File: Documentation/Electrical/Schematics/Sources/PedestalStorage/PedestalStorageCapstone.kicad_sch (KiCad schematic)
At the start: 2 parts

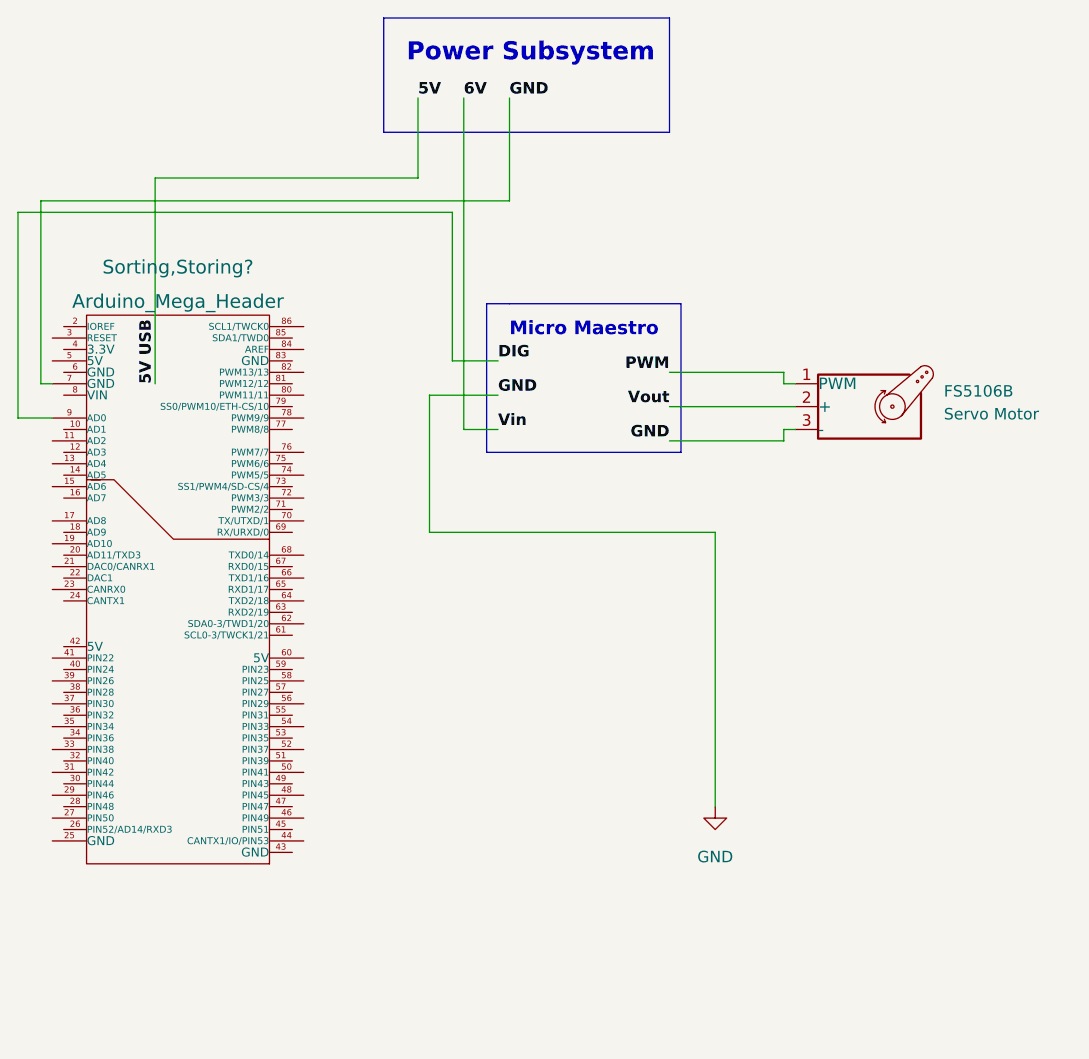
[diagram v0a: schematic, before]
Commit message: Deleted old circuit schenatic and added updated
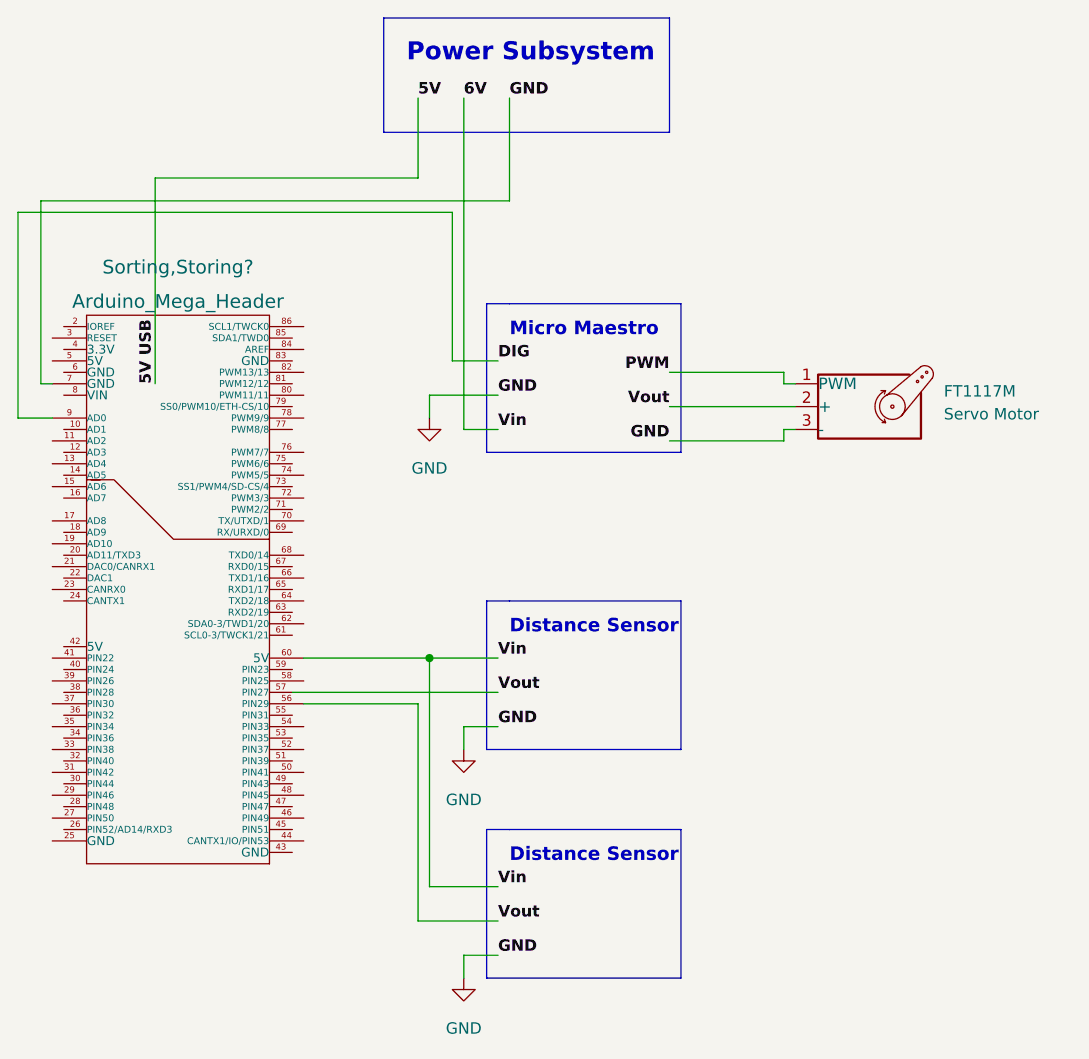
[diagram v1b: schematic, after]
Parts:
- renumbered FS5106B to FT1117M
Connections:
- net 6V: now also Sorting,Storing?.60 (5V)
- net Vout: now also Sorting,Storing?.56 (PIN29), Sorting,Storing?.57 (PIN27)
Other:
- note added: "Distance Sensor"
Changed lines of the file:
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@@
 (kicad_sch (version 20211123) (generator eeschema)
   (paper "A4")
+  (junction (at 99.06 102.87) (diameter 0) (color 0 0 0 0)
+  )
   (polyline (pts (xy 107.95 63.5) (xy 127 63.5))
     (stroke (width 0) (type solid) (color 0 0 0 0))
   )
+  (polyline (pts (xy 127 138.43) (xy 105.41 138.43))
+    (stroke (width 0) (type solid) (color 0 0 0 0))
+  )
   (wire (pts (xy 55.88 52.07) (xy 55.88 72.39))
     (stroke (width 0) (type default) (color 0 0 0 0))
@@
     (stroke (width 0) (type default) (color 0 0 0 0))
   )
-  (wire (pts (xy 130.81 88.9) (xy 130.81 119.38))
+  (wire (pts (xy 106.68 128.27) (xy 99.06 128.27))
+    (stroke (width 0) (type default) (color 0 0 0 0))
+  )
+  (wire (pts (xy 106.68 132.08) (xy 97.79 132.08))
     (stroke (width 0) (type default) (color 0 0 0 0))
   )
@@
     (stroke (width 0) (type default) (color 0 0 0 0))
   )
+  (polyline (pts (xy 127 121.92) (xy 127 138.43))
+    (stroke (width 0) (type solid) (color 0 0 0 0))
+  )
   (polyline (pts (xy 105.41 80.01) (xy 105.41 63.5))
     (stroke (width 0) (type solid) (color 0 0 0 0))
   )
-  (wire (pts (xy 99.06 88.9) (xy 130.81 88.9))
+  (polyline (pts (xy 105.41 113.03) (xy 105.41 96.52))
+    (stroke (width 0) (type solid) (color 0 0 0 0))
+  )
+  (wire (pts (xy 102.87 135.89) (xy 102.87 138.43))
     (stroke (width 0) (type default) (color 0 0 0 0))
   )
@@
     (stroke (width 0) (type default) (color 0 0 0 0))
   )
+  (polyline (pts (xy 127 113.03) (xy 105.41 113.03))
+    (stroke (width 0) (type solid) (color 0 0 0 0))
+  )
   (wire (pts (xy 57.15 76.2) (xy 53.34 76.2))
     (stroke (width 0) (type default) (color 0 0 0 0))
@@
     (stroke (width 0) (type default) (color 0 0 0 0))
   )
+  (wire (pts (xy 102.87 135.89) (xy 106.68 135.89))
+    (stroke (width 0) (type default) (color 0 0 0 0))
+  )
   (polyline (pts (xy 127 80.01) (xy 105.41 80.01))
     (stroke (width 0) (type solid) (color 0 0 0 0))
@@
     (stroke (width 0) (type default) (color 0 0 0 0))
   )
+  (wire (pts (xy 97.79 107.95) (xy 85.09 107.95))
+    (stroke (width 0) (type default) (color 0 0 0 0))
+  )
   (polyline (pts (xy 93.98 31.75) (xy 93.98 44.45))
     (stroke (width 0) (type default) (color 0 0 0 0))
   )
-  (wire (pts (xy 99.06 73.66) (xy 99.06 88.9))
-    (stroke (width 0) (type default) (color 0 0 0 0))
-  )
   (polyline (pts (xy 127 63.5) (xy 127 80.01))
     (stroke (width 0) (type solid) (color 0 0 0 0))
+  )
+  (wire (pts (xy 85.09 102.87) (xy 99.06 102.87))
+    (stroke (width 0) (type default) (color 0 0 0 0))
+  )
+  (wire (pts (xy 99.06 128.27) (xy 99.06 102.87))
+    (stroke (width 0) (type default) (color 0 0 0 0))
   )
   (wire (pts (xy 125.73 74.93) (xy 139.7 74.93))
     (stroke (width 0) (type default) (color 255 26 0 1))
   )
+  (polyline (pts (xy 107.95 96.52) (xy 127 96.52))
+    (stroke (width 0) (type solid) (color 0 0 0 0))
+  )
   (wire (pts (xy 53.34 53.34) (xy 101.6 53.34))
     (stroke (width 0) (type default) (color 0 0 0 0))
@@
     (stroke (width 0) (type default) (color 0 0 0 0))
   )
+  (wire (pts (xy 83.82 106.68) (xy 106.68 106.68))
+    (stroke (width 0) (type default) (color 0 0 0 0))
+  )
+  (polyline (pts (xy 107.95 121.92) (xy 127 121.92))
+    (stroke (width 0) (type solid) (color 0 0 0 0))
+  )
+  (polyline (pts (xy 105.41 121.92) (xy 107.95 121.92))
+    (stroke (width 0) (type solid) (color 0 0 0 0))
+  )
   (polyline (pts (xy 125.73 31.75) (xy 93.98 31.75))
     (stroke (width 0) (type default) (color 0 0 0 0))
   )
+  (polyline (pts (xy 105.41 96.52) (xy 107.95 96.52))
+    (stroke (width 0) (type solid) (color 0 0 0 0))
+  )
+  (wire (pts (xy 99.06 73.66) (xy 99.06 76.2))
+    (stroke (width 0) (type default) (color 0 0 0 0))
+  )
+  (wire (pts (xy 102.87 110.49) (xy 102.87 113.03))
+    (stroke (width 0) (type default) (color 0 0 0 0))
+  )
   (polyline (pts (xy 125.73 44.45) (xy 125.73 31.75))
     (stroke (width 0) (type default) (color 0 0 0 0))
   )
+  (wire (pts (xy 99.06 102.87) (xy 106.68 102.87))
+    (stroke (width 0) (type default) (color 0 0 0 0))
+  )
+  (polyline (pts (xy 105.41 138.43) (xy 105.41 121.92))
+    (stroke (width 0) (type solid) (color 0 0 0 0))
+  )
   (wire (pts (xy 97.79 49.53) (xy 68.58 49.53))
     (stroke (width 0) (type default) (color 0 0 0 0))
   )
+  (wire (pts (xy 97.79 132.08) (xy 97.79 107.95))
+    (stroke (width 0) (type default) (color 0 0 0 0))
+  )
   (wire (pts (xy 55.88 72.39) (xy 57.15 72.39))
     (stroke (width 0) (type default) (color 0 0 0 0))
   )
+  (polyline (pts (xy 127 96.52) (xy 127 113.03))
+    (stroke (width 0) (type solid) (color 0 0 0 0))
+  )
   (wire (pts (xy 102.87 77.47) (xy 106.68 77.47))
     (stroke (width 0) (type default) (color 0 0 0 0))
   )
   (wire (pts (xy 101.6 69.85) (xy 106.68 69.85))
+    (stroke (width 0) (type default) (color 0 0 0 0))
+  )
+  (wire (pts (xy 102.87 110.49) (xy 106.68 110.49))
     (stroke (width 0) (type default) (color 0 0 0 0))
   )
@@
     (effects (font (size 2 2) (thickness 0.4) bold) (justify left bottom))
   )
+  (text "Distance Sensor" (at 107.95 125.73 0)
+    (effects (font (size 1.5 1.5) (thickness 0.3) bold) (justify left bottom))
+  )
+  (text "Distance Sensor" (at 107.95 100.33 0)
+    (effects (font (size 1.5 1.5) (thickness 0.3) bold) (justify left bottom))
+  )
   (text "Micro Maestro" (at 107.95 67.31 0)
     (effects (font (size 1.5 1.5) (thickness 0.3) bold) (justify left bottom))
@@
     (effects (font (size 1.27 1.27) (thickness 0.254) bold) (justify left bottom))
   )
+  (label "GND" (at 106.68 110.49 0)
+    (effects (font (size 1.27 1.27) (thickness 0.254) bold) (justify left bottom))
+  )
+  (label "Vin" (at 106.68 102.87 0)
+    (effects (font (size 1.27 1.27) (thickness 0.254) bold) (justify left bottom))
+  )
   (label "PWM" (at 125.73 71.12 180)
     (effects (font (size 1.27 1.27) (thickness 0.254) bold) (justify right bottom))
   )
+  (label "Vout" (at 106.68 132.08 0)
+    (effects (font (size 1.27 1.27) (thickness 0.254) bold) (justify left bottom))
+  )
+  (label "Vout" (at 106.68 106.68 0)
+    (effects (font (size 1.27 1.27) (thickness 0.254) bold) (justify left bottom))
+  )
   (label "GND" (at 106.68 73.66 0)
     (effects (font (size 1.27 1.27) (thickness 0.254) bold) (justify left bottom))
@@
   )
   (label "DIG" (at 106.68 69.85 0)
+    (effects (font (size 1.27 1.27) (thickness 0.254) bold) (justify left bottom))
+  )
+  (label "Vin" (at 106.68 128.27 0)
     (effects (font (size 1.27 1.27) (thickness 0.254) bold) (justify left bottom))
   )
@@
     (effects (font (size 1.27 1.27) (thickness 0.254) bold) (justify left bottom))
   )
+  (label "GND" (at 106.68 135.89 0)
+    (effects (font (size 1.27 1.27) (thickness 0.254) bold) (justify left bottom))
+  )
   (symbol (lib_id "Motor:Motor_Servo") (at 147.32 74.93 0) (unit 1)
     (in_bom yes) (on_board yes) (fields_autoplaced)
-    (property "Reference" "FS5106B" (id 0) (at 156.21 73.2265 0)
+    (property "Reference" "FT1117M" (id 0) (at 156.21 73.2265 0)
       (effects (font (size 1.27 1.27)) (justify left))
     )
@@
     (pin "3")
   )
-  (symbol (lib_id "power:GND") (at 130.81 119.38 0) (unit 1)
+  (symbol (lib_id "power:GND") (at 102.87 138.43 0) (unit 1)
     (in_bom yes) (on_board yes) (fields_autoplaced)
-    (property "Reference" "#PWR?" (id 0) (at 130.81 125.73 0)
-      (effects (font (size 1.27 1.27)) hide)
-    )
-    (property "Value" "GND" (id 1) (at 130.81 124.968 0))
-    (property "Footprint" "" (id 2) (at 130.81 119.38 0)
-      (effects (font (size 1.27 1.27)) hide)
-    )
-    (property "Datasheet" "" (id 3) (at 130.81 119.38 0)
+    (property "Reference" "#PWR?" (id 0) (at 102.87 144.78 0)
+      (effects (font (size 1.27 1.27)) hide)
+    )
+    (property "Value" "GND" (id 1) (at 102.87 144.018 0))
+    (property "Footprint" "" (id 2) (at 102.87 138.43 0)
+      (effects (font (size 1.27 1.27)) hide)
+    )
+    (property "Datasheet" "" (id 3) (at 102.87 138.43 0)
+      (effects (font (size 1.27 1.27)) hide)
+    )
+    (pin "1")
+  )
+  (symbol (lib_id "power:GND") (at 99.06 76.2 0) (unit 1)
+    (in_bom yes) (on_board yes) (fields_autoplaced)
+    (property "Reference" "#PWR?" (id 0) (at 99.06 82.55 0)
+      (effects (font (size 1.27 1.27)) hide)
+    )
+    (property "Value" "GND" (id 1) (at 99.06 81.788 0))
+    (property "Footprint" "" (id 2) (at 99.06 76.2 0)
+      (effects (font (size 1.27 1.27)) hide)
+    )
+    (property "Datasheet" "" (id 3) (at 99.06 76.2 0)
+      (effects (font (size 1.27 1.27)) hide)
+    )
+    (pin "1")
+  )
+  (symbol (lib_id "power:GND") (at 102.87 113.03 0) (unit 1)
+    (in_bom yes) (on_board yes) (fields_autoplaced)
+    (property "Reference" "#PWR?" (id 0) (at 102.87 119.38 0)
+      (effects (font (size 1.27 1.27)) hide)
+    )
+    (property "Value" "GND" (id 1) (at 102.87 118.618 0))
+    (property "Footprint" "" (id 2) (at 102.87 113.03 0)
+      (effects (font (size 1.27 1.27)) hide)
+    )
+    (property "Datasheet" "" (id 3) (at 102.87 113.03 0)
       (effects (font (size 1.27 1.27)) hide)
     )
@@
   )
   (symbol_instances
+    (path "/156582d9-61dd-46da-b34f-489d526b9cc4"
+      (reference "#PWR?") (unit 1) (value "GND") (footprint "")
+    )
     (path "/20191c58-9ee2-4cf1-9ddd-02e1cf219d6f"
       (reference "#PWR?") (unit 1) (value "GND") (footprint "")
     )
+    (path "/b64ba7b8-bcbe-4c99-a3af-8b2afaa709b2"
+      (reference "#PWR?") (unit 1) (value "GND") (footprint "")
+    )
     (path "/00797e88-c5f5-495f-a97a-b43ec13784f9"
-      (reference "FS5106B") (unit 1) (value "Servo Motor") (footprint "")
+      (reference "FT1117M") (unit 1) (value "Servo Motor") (footprint "")
     )
     (path "/d7b32df9-2b5c-453e-948e-7bad0b979c0f"

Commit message: Updated electrical schematic
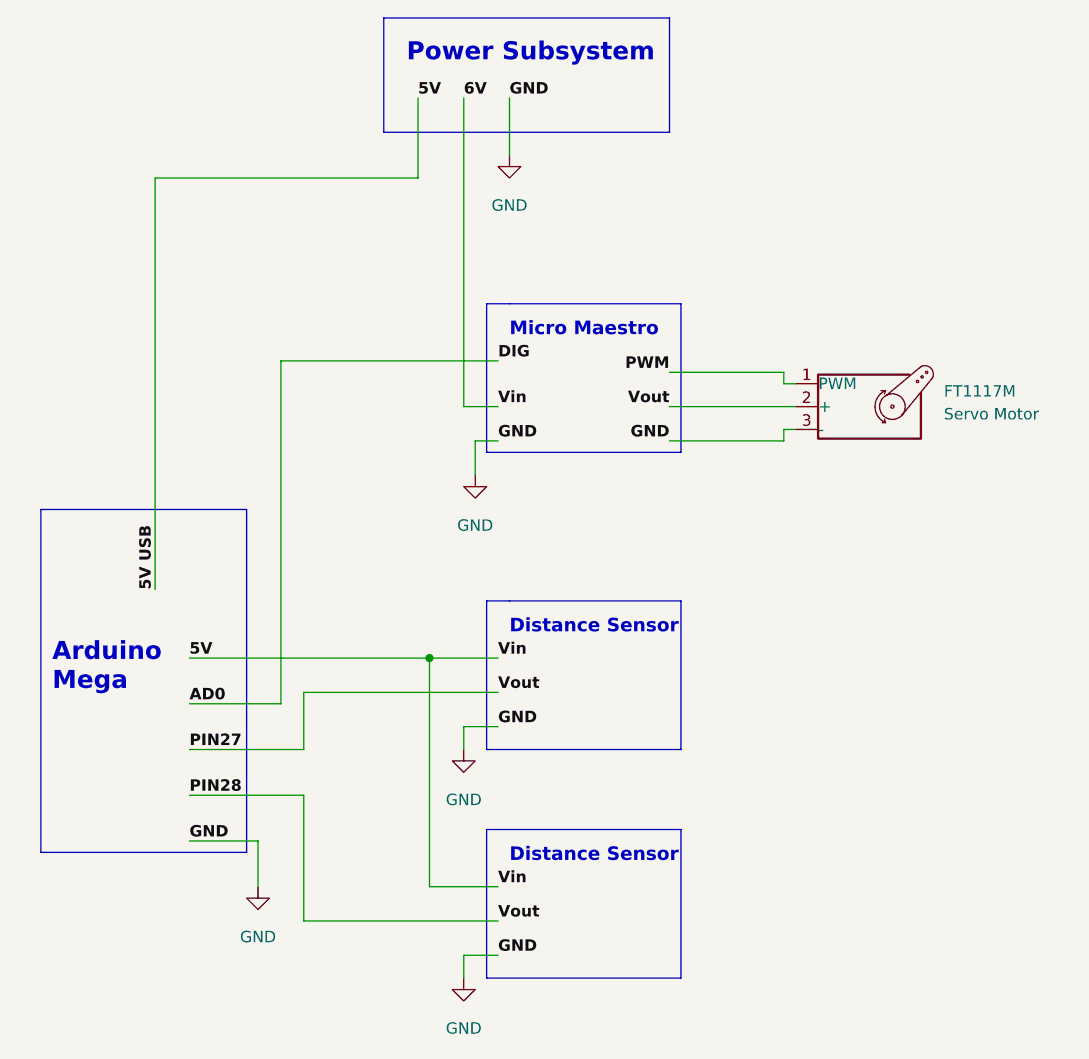
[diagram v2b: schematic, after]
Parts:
- removed Sorting,Storing?: Arduino_Mega_Header, symbol w_connectors:Arduino_Mega_Header
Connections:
- net Vout renamed PIN27
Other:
- note added: "Arduino Mega"
